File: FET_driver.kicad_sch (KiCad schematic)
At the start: 48 parts, among them Q1 TPH3R704PL,L1Q, Q10 TPH3R704PL,L1Q, Q11 TPH3R704PL,L1Q, Q12 TPH3R704PL,L1Q, Q2 TPH3R704PL,L1Q, Q3 TPH3R704PL,L1Q, Q4 TPH3R704PL,L1Q, Q5 TPH3R704PL,L1Q, Q6 TPH3R704PL,L1Q, Q7 TPH3R704PL,L1Q, Q8 TPH3R704PL,L1Q, Q9 TPH3R704PL,L1Q, U7 FD6288Q, U8 FD6288Q

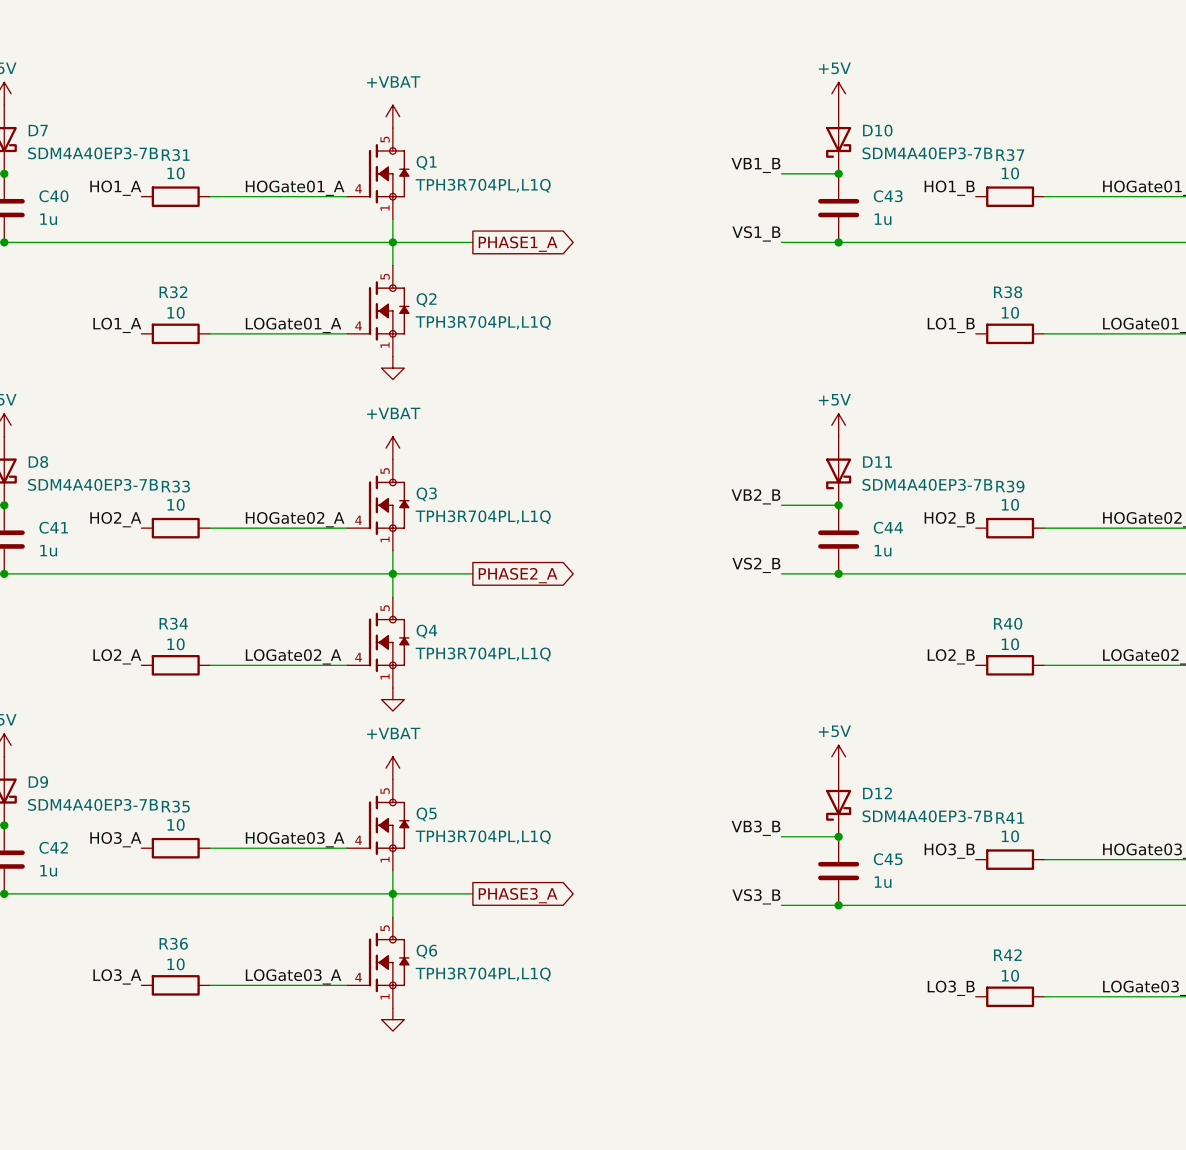
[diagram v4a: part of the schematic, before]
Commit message: cleanup BOM and bump up voltage rating/footprint for capacitors to max possible
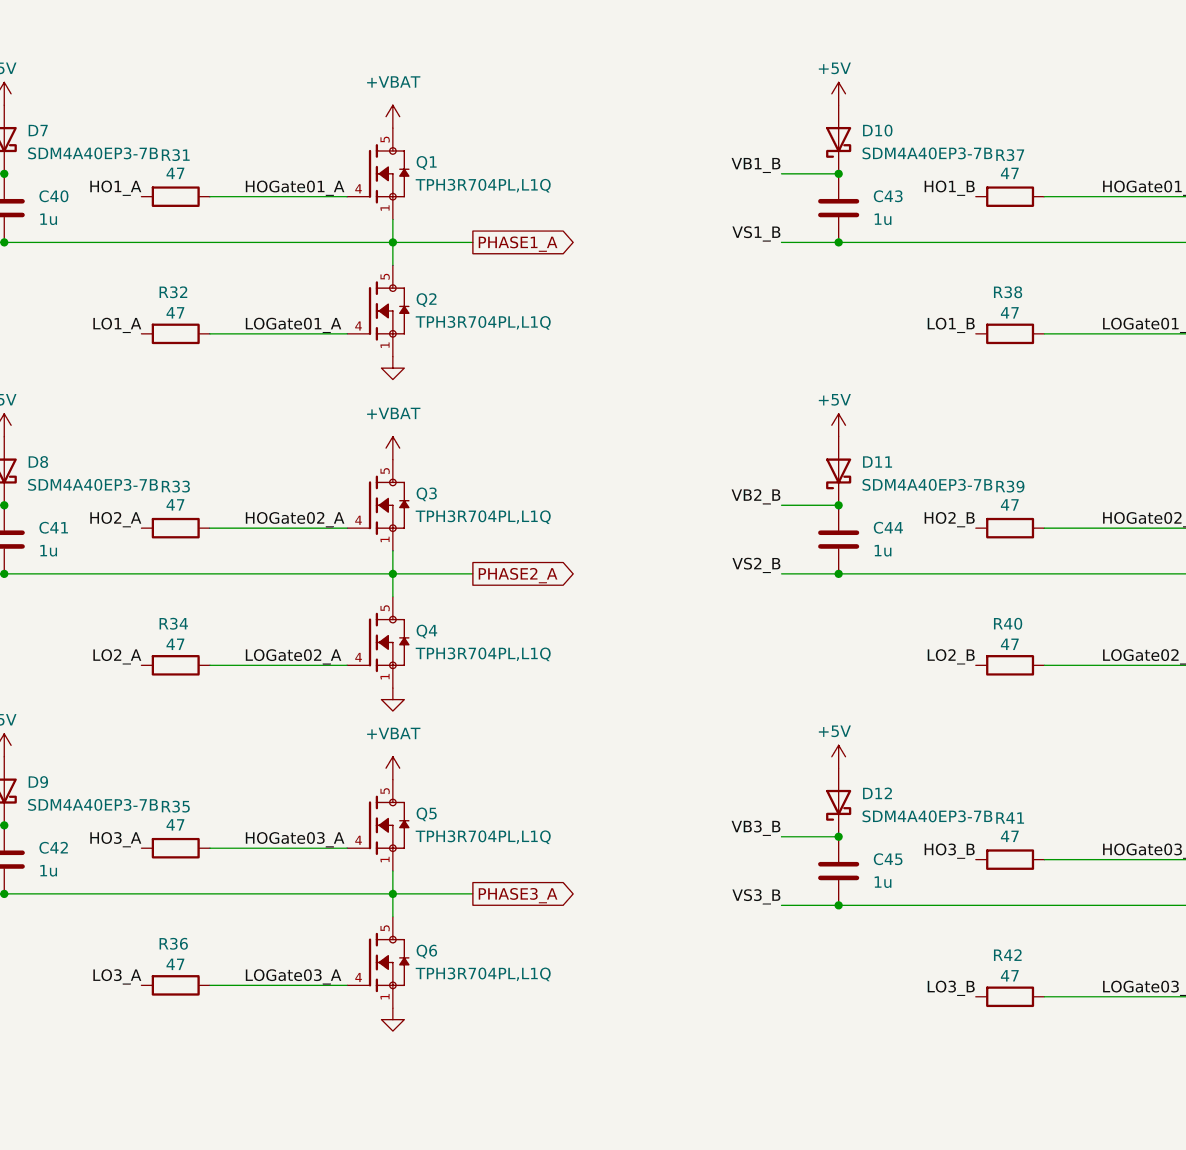
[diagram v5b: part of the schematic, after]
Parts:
- C36, C38: Manufacturer YAGEO -> Murata; Part Number CC0402KRX5R7BB104 -> GRM155R61H104KE14D; Voltage 16 -> 50
- C37, C39: footprint Capacitor_SMD:C_0402_1005Metric -> Capacitor_SMD:C_0805_2012Metric; Manufacturer YAGEO -> Murata; Part Number GRM155R61E102KA01D -> GRM21BR61H106KE43L; Voltage 10 -> 50
- D10, D11, D12, D7, D8, D9: Note (none) -> SDT4U40EP3-7B
- R31, R32, R33, R34, R35, R36, R37, R38, R39, R40, R41, R42: value 10 -> 47; Part Number RC0603FR-0710RL -> RC0603FR-0747RL
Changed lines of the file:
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@@
 			)
 		)
-		(property "Datasheet" "~"
+		(property "Datasheet" "https://www.diodes.com/assets/Datasheets/SDM4A40EP3.pdf"
 			(at 118.11 52.07 0)
 			(effects
@@
 			)
 		)
+		(property "Note" "SDT4U40EP3-7B "
+			(at 118.11 52.07 0)
+			(effects
+				(font
+					(size 1.27 1.27)
+				)
+				(hide yes)
+			)
+		)
 		(pin "2"
 		)
@@
 			)
 		)
-		(property "Footprint" "Capacitor_SMD:C_0402_1005Metric"
+		(property "Footprint" "Capacitor_SMD:C_0805_2012Metric"
 			(at 92.4052 109.22 0)
 			(effects
@@
 			)
 		)
-		(property "Part Number" "GRM155R61E102KA01D"
+		(property "Part Number" "GRM21BR61H106KE43L"
 			(at 91.44 105.41 0)
 			(effects
@@
 			)
 		)
-		(property "Manufacturer" "YAGEO"
+		(property "Manufacturer" "Murata"
 			(at 91.44 105.41 0)
 			(effects
@@
 			)
 		)
-		(property "Voltage" "10"
+		(property "Voltage" "50"
 			(at 91.44 105.41 0)
 			(effects
@@
 			)
 		)
-		(property "Datasheet" "~"
+		(property "Datasheet" "https://www.diodes.com/assets/Datasheets/SDM4A40EP3.pdf"
 			(at 118.11 88.9 0)
 			(effects
@@
 			)
 		)
+		(property "Note" "SDT4U40EP3-7B "
+			(at 118.11 88.9 0)
+			(effects
+				(font
+					(size 1.27 1.27)
+				)
+				(hide yes)
+			)
+		)
 		(pin "2"
 		)
@@
 			)
 		)
-		(property "Value" "10"
+		(property "Value" "47"
 			(at 229.87 108.204 90)
 			(effects
@@
 			)
 		)
-		(property "Part Number" "RC0603FR-0710RL"
+		(property "Part Number" "RC0603FR-0747RL"
 			(at 229.87 110.49 0)
 			(effects
@@
 			)
 		)
-		(property "Value" "10"
+		(property "Value" "47"
 			(at 137.16 143.764 90)
 			(effects
@@
 			)
 		)
-		(property "Part Number" "RC0603FR-0710RL"
+		(property "Part Number" "RC0603FR-0747RL"
 			(at 137.16 146.05 0)
 			(effects
@@
 			)
 		)
-		(property "Datasheet" "~"
+		(property "Datasheet" "https://www.diodes.com/assets/Datasheets/SDM4A40EP3.pdf"
 			(at 210.82 52.07 0)
 			(effects
@@
 			)
 		)
+		(property "Note" "SDT4U40EP3-7B "
+			(at 210.82 52.07 0)
+			(effects
+				(font
+					(size 1.27 1.27)
+				)
+				(hide yes)
+			)
+		)
 		(pin "2"
 		)
@@
 			)
 		)
-		(property "Value" "10"
+		(property "Value" "47"
 			(at 137.16 108.204 90)
 			(effects
@@
 			)
 		)
-		(property "Part Number" "RC0603FR-0710RL"
+		(property "Part Number" "RC0603FR-0747RL"
 			(at 137.16 110.49 0)
 			(effects
@@
 			)
 		)
-		(property "Datasheet" ""
+		(property "Datasheet" "https://static.qingshow.net/fortiortech/file/1597746029372.pdf"
 			(at 50.8 50.8 0)
 			(effects
@@
 			)
 		)
-		(property "Value" "10"
+		(property "Value" "47"
 			(at 137.16 71.374 90)
 			(effects
@@
 			)
 		)
-		(property "Part Number" "RC0603FR-0710RL"
+		(property "Part Number" "RC0603FR-0747RL"
 			(at 137.16 73.66 0)
 			(effects
@@
 			)
 		)
-		(property "Value" "10"
+		(property "Value" "47"
 			(at 229.87 55.88 90)
 			(effects
@@
 			)
 		)
-		(property "Part Number" "RC0603FR-0710RL"
+		(property "Part Number" "RC0603FR-0747RL"
 			(at 229.87 58.42 0)
 			(effects
@@
 			)
 		)
-		(property "Value" "10"
+		(property "Value" "47"
 			(at 229.87 92.71 90)
 			(effects
@@
 			)
 		)
-		(property "Part Number" "RC0603FR-0710RL"
+		(property "Part Number" "RC0603FR-0747RL"
 			(at 229.87 95.25 0)
 			(effects
@@
 			)
 		)
-		(property "Datasheet" "~"
+		(property "Datasheet" "https://www.diodes.com/assets/Datasheets/SDM4A40EP3.pdf"
 			(at 210.82 125.73 0)
 			(effects
@@
 			)
 		)
+		(property "Note" "SDT4U40EP3-7B "
+			(at 210.82 125.73 0)
+			(effects
+				(font
+					(size 1.27 1.27)
+				)
+				(hide yes)
+			)
+		)
 		(pin "2"
 		)
@@
 			)
 		)
-		(property "Part Number" "CC0402KRX5R7BB104"
+		(property "Part Number" "GRM155R61H104KE14D"
 			(at 80.01 105.41 0)
 			(effects
@@
 			)
 		)
-		(property "Manufacturer" "YAGEO"
+		(property "Manufacturer" "Murata"
 			(at 80.01 105.41 0)
 			(effects
@@
 			)
 		)
-		(property "Voltage" "16"
+		(property "Voltage" "50"
 			(at 80.01 105.41 0)
 			(effects
@@
 			)
 		)
-		(property "Datasheet" "~"
+		(property "Datasheet" "https://www.diodes.com/assets/Datasheets/SDM4A40EP3.pdf"
 			(at 118.11 124.46 0)
 			(effects
@@
 			)
 		)
+		(property "Note" "SDT4U40EP3-7B "
+			(at 118.11 124.46 0)
+			(effects
+				(font
+					(size 1.27 1.27)
+				)
+				(hide yes)
+			)
+		)
 		(pin "2"
 		)
@@
 			)
 		)
-		(property "Value" "10"
+		(property "Value" "47"
 			(at 229.87 129.54 90)
 			(effects
@@
 			)
 		)
-		(property "Part Number" "RC0603FR-0710RL"
+		(property "Part Number" "RC0603FR-0747RL"
 			(at 229.87 132.08 0)
 			(effects
@@
 			)
 		)
-		(property "Datasheet" "~"
+		(property "Datasheet" "https://www.diodes.com/assets/Datasheets/SDM4A40EP3.pdf"
 			(at 210.82 88.9 0)
 			(effects
@@
 			)
 		)
+		(property "Note" "SDT4U40EP3-7B "
+			(at 210.82 88.9 0)
+			(effects
+				(font
+					(size 1.27 1.27)
+				)
+				(hide yes)
+			)
+		)
 		(pin "2"
 		)
@@
 			)
 		)
-		(property "Value" "10"
+		(property "Value" "47"
 			(at 137.16 55.88 90)
 			(effects
@@
 			)
 		)
-		(property "Part Number" "RC0603FR-0710RL"
+		(property "Part Number" "RC0603FR-0747RL"
 			(at 137.16 58.42 0)
 			(effects
@@
 			)
 		)
-		(property "Value" "10"
+		(property "Value" "47"
 			(at 137.16 128.27 90)
 			(effects
@@
 			)
 		)
-		(property "Part Number" "RC0603FR-0710RL"
+		(property "Part Number" "RC0603FR-0747RL"
 			(at 137.16 130.81 0)
 			(effects
@@
 			)
 		)
-		(property "Footprint" "Capacitor_SMD:C_0402_1005Metric"
+		(property "Footprint" "Capacitor_SMD:C_0805_2012Metric"
 			(at 92.4052 35.56 0)
 			(effects
@@
 			)
 		)
-		(property "Part Number" "GRM155R61E102KA01D"
+		(property "Part Number" "GRM21BR61H106KE43L"
 			(at 91.44 31.75 0)
 			(effects
@@
 			)
 		)
-		(property "Manufacturer" "YAGEO"
+		(property "Manufacturer" "Murata"
 			(at 91.44 31.75 0)
 			(effects
@@
 			)
 		)
-		(property "Voltage" "10"
+		(property "Voltage" "50"
 			(at 91.44 31.75 0)
 			(effects
@@
 			)
 		)
-		(property "Value" "10"
+		(property "Value" "47"
 			(at 229.87 145.034 90)
 			(effects
@@
 			)
 		)
-		(property "Part Number" "RC0603FR-0710RL"
+		(property "Part Number" "RC0603FR-0747RL"
 			(at 229.87 147.32 0)
 			(effects
@@
 			)
 		)
-		(property "Value" "10"
+		(property "Value" "47"
 			(at 137.16 92.71 90)
 			(effects
@@
 			)
 		)
-		(property "Part Number" "RC0603FR-0710RL"
+		(property "Part Number" "RC0603FR-0747RL"
 			(at 137.16 95.25 0)
 			(effects
@@
 			)
 		)
-		(property "Value" "10"
+		(property "Value" "47"
 			(at 229.87 71.374 90)
 			(effects
@@
 			)
 		)
-		(property "Part Number" "RC0603FR-0710RL"
+		(property "Part Number" "RC0603FR-0747RL"
 			(at 229.87 73.66 0)
 			(effects
@@
 			)
 		)
-		(property "Part Number" "CC0402KRX5R7BB104"
+		(property "Part Number" "GRM155R61H104KE14D"
 			(at 80.01 31.75 0)
 			(effects
@@
 			)
 		)
-		(property "Manufacturer" "YAGEO"
+		(property "Manufacturer" "Murata"
 			(at 80.01 31.75 0)
 			(effects
@@
 			)
 		)
-		(property "Voltage" "16"
+		(property "Voltage" "50"
 			(at 80.01 31.75 0)
 			(effects
@@
 			)
 		)
-		(property "Datasheet" ""
+		(property "Datasheet" "https://static.qingshow.net/fortiortech/file/1597746029372.pdf"
 			(at 50.8 124.46 0)
 			(effects
